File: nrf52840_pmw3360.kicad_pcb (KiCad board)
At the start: 2 copper layers, 18 x 33 mm, 3 parts, among them J1 PMW3360_Breakout, J2 Battery_JST-PH, U1 SuperMini_nRF52840

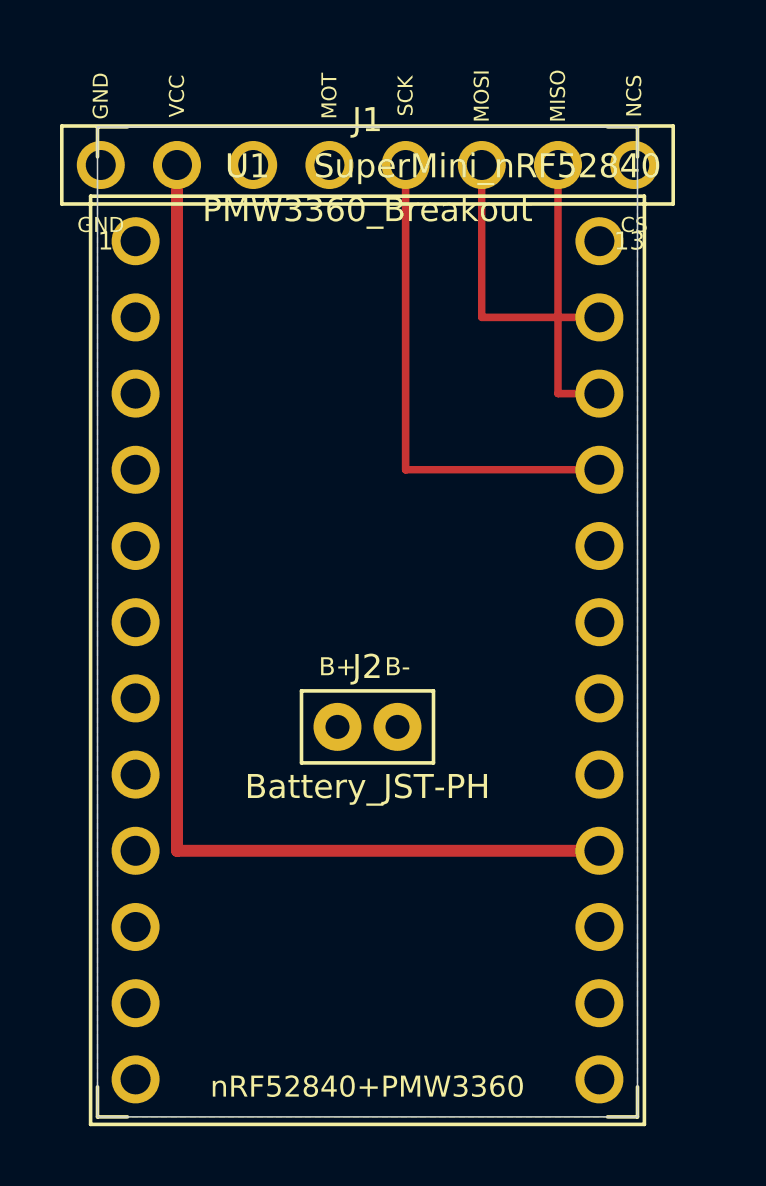
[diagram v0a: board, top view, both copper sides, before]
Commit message: feat: NCS・MOTION・BATIN未配線ネットをPCBに配線
- NCS: J1[8]→B.Cu右端→底辺→U1Lpin12 (周回ルート)
- MOTION: J1[4]→B.Cu縦→U1Lpin11 (L字ルート)
- BATIN: J2[1]→F.Cu縦→U1Rpin24 (L字ルート)
- J2バッテリーコネクタ: 左中央(x=4.5, y=16.5mm)に配置
- 全ネット配線完了: MOSI/MISO/SCK/VCC/BATIN(F.Cu) + NCS/MOTION(B.Cu)

Co-Authored-By: Claude Sonnet 4.6 <noreply@anthropic.com>
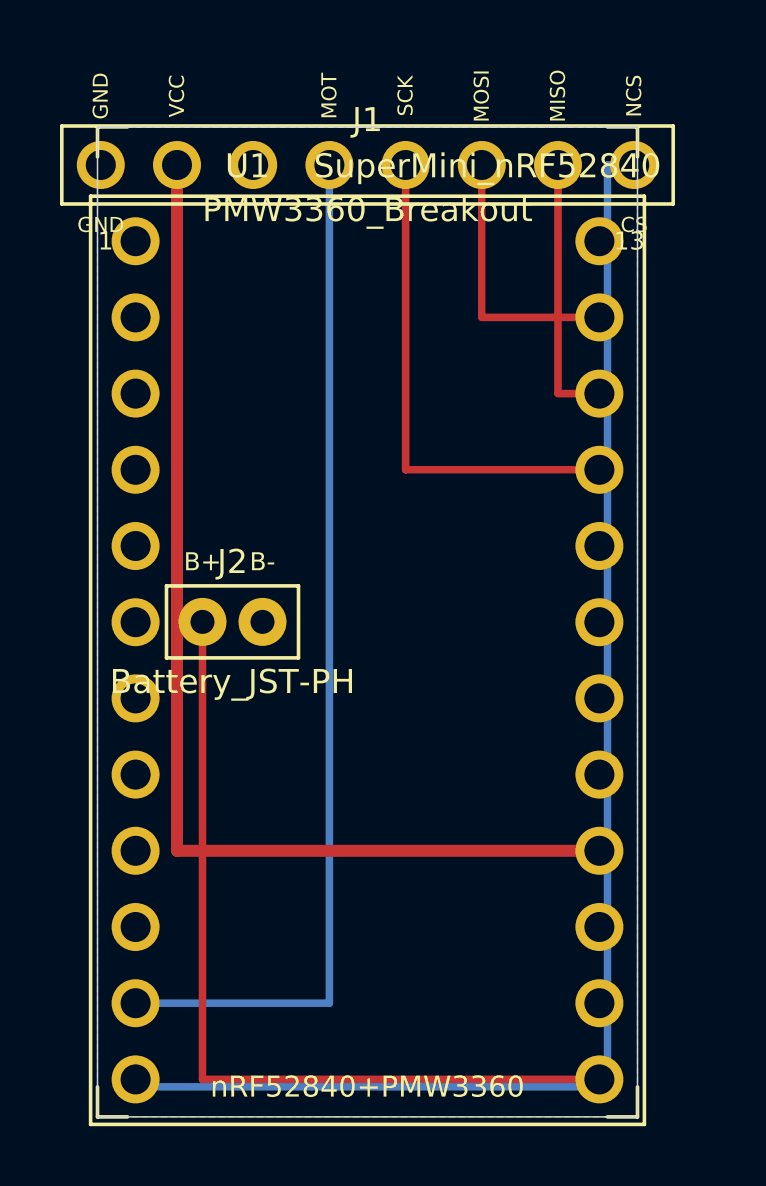
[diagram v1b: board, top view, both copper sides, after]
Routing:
- net NCS: track 0.00 -> 47.6 mm
- net MOTION: track 0.00 -> 34.4 mm
- net BATIN: track 0.00 -> 28.5 mm
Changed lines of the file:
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@@
 )
 (footprint "Connector_JST_PH_2pin" (layer "F.Cu") (at 0 0)
-  (fp_text reference "J2" (at 9.0000 18.0000) (layer "F.SilkS")
+  (fp_text reference "J2" (at 4.5000 14.5000) (layer "F.SilkS")
     (effects (font (size 0.8 0.8) (thickness 0.15))))
-  (fp_text value "Battery_JST-PH" (at 9.0000 22.0000) (layer "F.SilkS")
+  (fp_text value "Battery_JST-PH" (at 4.5000 18.5000) (layer "F.SilkS")
     (effects (font (size 0.8 0.8) (thickness 0.15))))
-    (pad "1" thru_hole oval (at 8.0000 20.0000) (size 1.6000 1.6000) (drill 0.8000) (layers "*.Cu" "*.Mask") (net 8 "BATIN"))
-    (pad "2" thru_hole circle (at 10.0000 20.0000) (size 1.6000 1.6000) (drill 0.8000) (layers "*.Cu" "*.Mask") (net 1 "GND"))
-  (fp_line (start 6.5500 18.5500) (end 11.4500 18.5500) (stroke (width 0.0500) (type default)) (layer "F.CrtYd"))
-  (fp_line (start 11.4500 18.5500) (end 11.4500 21.4500) (stroke (width 0.0500) (type default)) (layer "F.CrtYd"))
-  (fp_line (start 11.4500 21.4500) (end 6.5500 21.4500) (stroke (width 0.0500) (type default)) (layer "F.CrtYd"))
-  (fp_line (start 6.5500 21.4500) (end 6.5500 18.5500) (stroke (width 0.0500) (type default)) (layer "F.CrtYd"))
-  (fp_line (start 6.8000 18.8000) (end 11.2000 18.8000) (stroke (width 0.1200) (type default)) (layer "F.SilkS"))
-  (fp_line (start 11.2000 18.8000) (end 11.2000 21.2000) (stroke (width 0.1200) (type default)) (layer "F.SilkS"))
-  (fp_line (start 11.2000 21.2000) (end 6.8000 21.2000) (stroke (width 0.1200) (type default)) (layer "F.SilkS"))
-  (fp_line (start 6.8000 21.2000) (end 6.8000 18.8000) (stroke (width 0.1200) (type default)) (layer "F.SilkS"))
-  (fp_text user "B+" (at 8.0000 18.0000) (layer "F.SilkS")
+    (pad "1" thru_hole oval (at 3.5000 16.5000) (size 1.6000 1.6000) (drill 0.8000) (layers "*.Cu" "*.Mask") (net 8 "BATIN"))
+    (pad "2" thru_hole circle (at 5.5000 16.5000) (size 1.6000 1.6000) (drill 0.8000) (layers "*.Cu" "*.Mask") (net 1 "GND"))
+  (fp_line (start 2.0500 15.0500) (end 6.9500 15.0500) (stroke (width 0.0500) (type default)) (layer "F.CrtYd"))
+  (fp_line (start 6.9500 15.0500) (end 6.9500 17.9500) (stroke (width 0.0500) (type default)) (layer "F.CrtYd"))
+  (fp_line (start 6.9500 17.9500) (end 2.0500 17.9500) (stroke (width 0.0500) (type default)) (layer "F.CrtYd"))
+  (fp_line (start 2.0500 17.9500) (end 2.0500 15.0500) (stroke (width 0.0500) (type default)) (layer "F.CrtYd"))
+  (fp_line (start 2.3000 15.3000) (end 6.7000 15.3000) (stroke (width 0.1200) (type default)) (layer "F.SilkS"))
+  (fp_line (start 6.7000 15.3000) (end 6.7000 17.7000) (stroke (width 0.1200) (type default)) (layer "F.SilkS"))
+  (fp_line (start 6.7000 17.7000) (end 2.3000 17.7000) (stroke (width 0.1200) (type default)) (layer "F.SilkS"))
+  (fp_line (start 2.3000 17.7000) (end 2.3000 15.3000) (stroke (width 0.1200) (type default)) (layer "F.SilkS"))
+  (fp_text user "B+" (at 3.5000 14.5000) (layer "F.SilkS")
     (effects (font (size 0.6 0.6) (thickness 0.15))))
-  (fp_text user "B-" (at 10.0000 18.0000) (layer "F.SilkS")
+  (fp_text user "B-" (at 5.5000 14.5000) (layer "F.SilkS")
     (effects (font (size 0.6 0.6) (thickness 0.15))))
 )
@@
 (segment (start 2.6500 1.2700) (end 2.6500 24.1300) (width 0.4000) (layer "F.Cu") (net 2))
 (segment (start 2.6500 24.1300) (end 16.7300 24.1300) (width 0.4000) (layer "F.Cu") (net 2))
+(segment (start 3.5000 16.5000) (end 3.5000 31.7500) (width 0.2500) (layer "F.Cu") (net 8))
+(segment (start 3.5000 31.7500) (end 16.7300 31.7500) (width 0.2500) (layer "F.Cu") (net 8))
+(segment (start 17.8900 1.2700) (end 17.0000 1.2700) (width 0.2500) (layer "B.Cu") (net 6))
+(segment (start 17.0000 1.2700) (end 17.0000 32.0000) (width 0.2500) (layer "B.Cu") (net 6))
+(segment (start 17.0000 32.0000) (end 1.2700 32.0000) (width 0.2500) (layer "B.Cu") (net 6))
+(segment (start 1.2700 32.0000) (end 1.2700 31.7500) (width 0.2500) (layer "B.Cu") (net 6))
+(segment (start 7.7300 1.2700) (end 7.7300 29.2100) (width 0.2500) (layer "B.Cu") (net 7))
+(segment (start 7.7300 29.2100) (end 1.2700 29.2100) (width 0.2500) (layer "B.Cu") (net 7))
 (zone (net 1) (net_name "GND") (layer "B.Cu")
   (hatch edge 0.508)

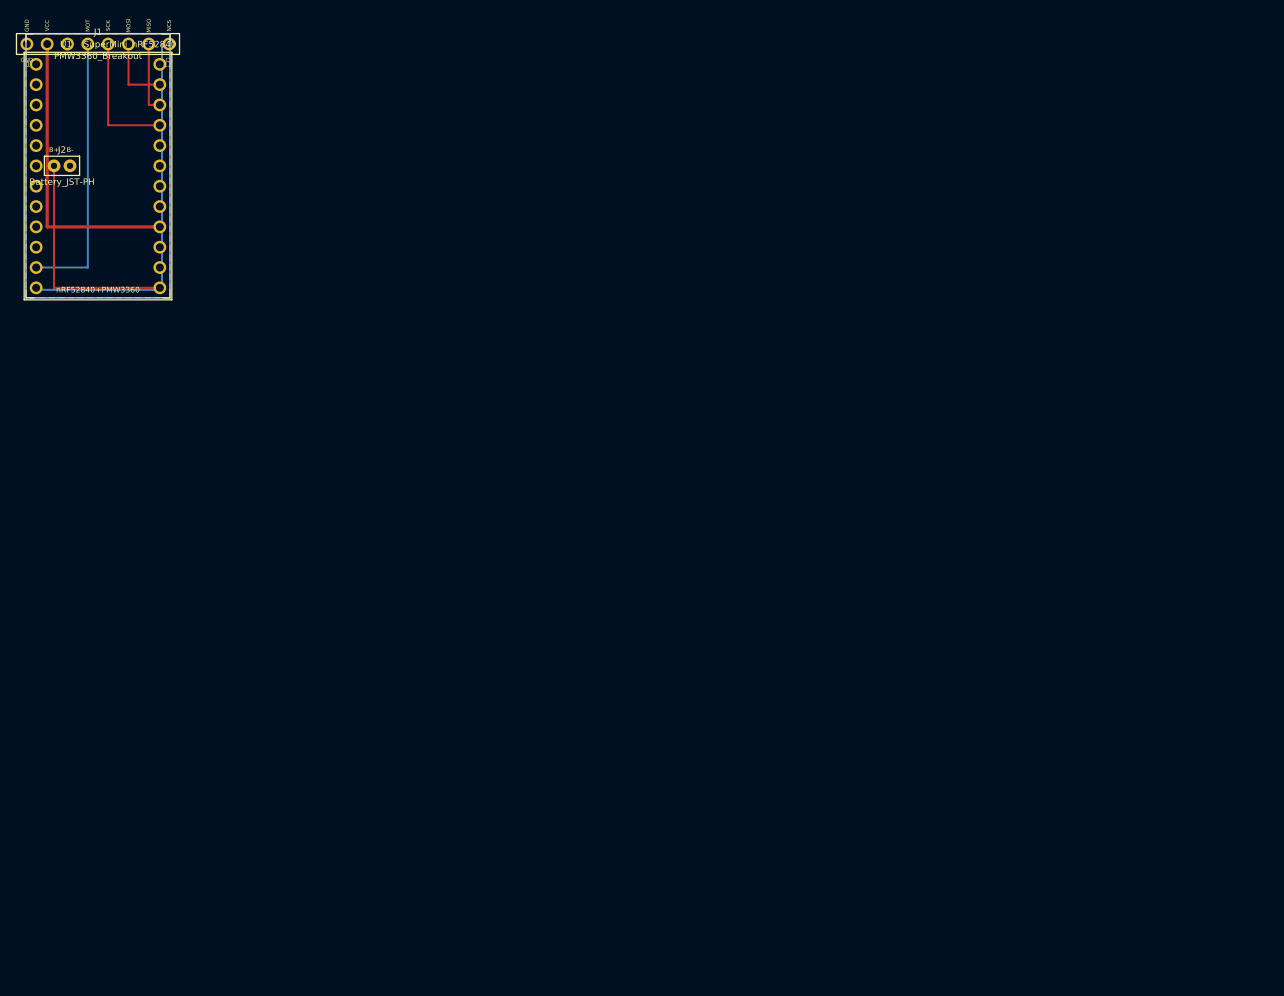
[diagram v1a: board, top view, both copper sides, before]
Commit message: fix: ボードをA4ページ中央(135,85mm)に配置、左上表示を修正
KiCadで開いたとき原点(0,0)＝左上隅に表示される問題を修正。
ORIGIN_X=135, ORIGIN_Y=85 のオフセットを全座標に適用。

Co-Authored-By: Claude Sonnet 4.6 <noreply@anthropic.com>
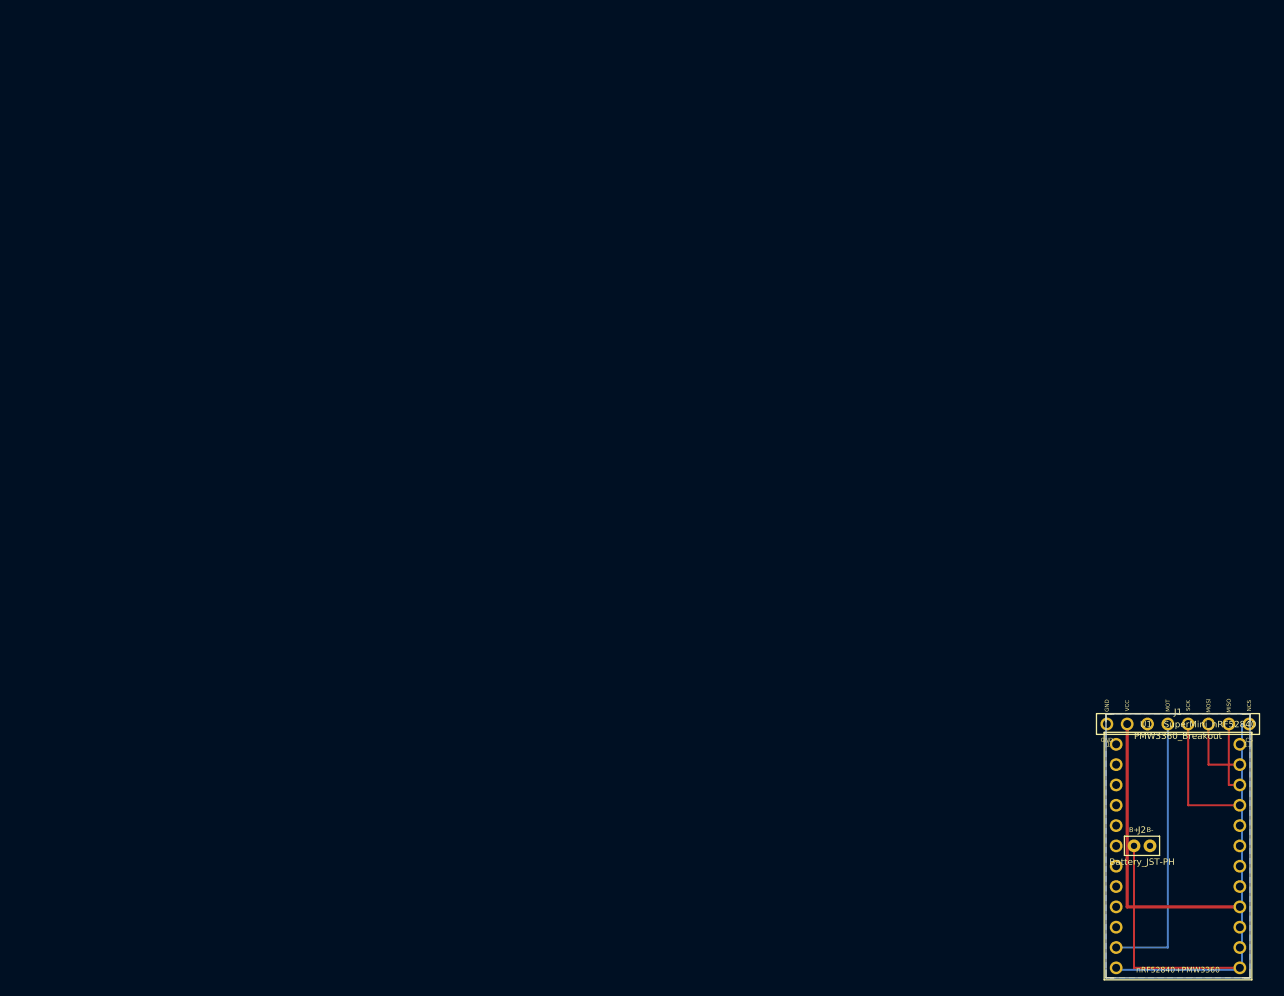
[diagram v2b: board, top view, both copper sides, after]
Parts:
- moved J1 159.5 mm to (135.0, 85.0)
- moved J2 159.5 mm to (135.0, 85.0)
- moved U1 159.5 mm to (135.0, 85.0)
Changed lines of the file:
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@@
   (net 7 "MOTION")
   (net 8 "BATIN")
-  (gr_rect (start 0 0) (end 18.0000 33.0000) (stroke (width 0.05) (type default)) (layer "Edge.Cuts"))
-  (gr_line (start 0.00 0.00) (end 1.00 0.00) (stroke (width 0.12) (type default)) (layer "F.SilkS"))
-  (gr_line (start 0.00 0.00) (end 0.00 1.00) (stroke (width 0.12) (type default)) (layer "F.SilkS"))
-  (gr_line (start 18.00 0.00) (end 17.00 0.00) (stroke (width 0.12) (type default)) (layer "F.SilkS"))
-  (gr_line (start 18.00 0.00) (end 18.00 1.00) (stroke (width 0.12) (type default)) (layer "F.SilkS"))
-  (gr_line (start 18.00 33.00) (end 17.00 33.00) (stroke (width 0.12) (type default)) (layer "F.SilkS"))
-  (gr_line (start 18.00 33.00) (end 18.00 32.00) (stroke (width 0.12) (type default)) (layer "F.SilkS"))
-  (gr_line (start 0.00 33.00) (end 1.00 33.00) (stroke (width 0.12) (type default)) (layer "F.SilkS"))
-  (gr_line (start 0.00 33.00) (end 0.00 32.00) (stroke (width 0.12) (type default)) (layer "F.SilkS"))
-(footprint "SuperMini_nRF52840_Socket" (layer "F.Cu") (at 0 0)
+  (gr_rect (start 135.0000 85.0000) (end 153.0000 118.0000) (stroke (width 0.05) (type default)) (layer "Edge.Cuts"))
+  (gr_line (start 135.00 85.00) (end 136.00 85.00) (stroke (width 0.12) (type default)) (layer "F.SilkS"))
+  (gr_line (start 135.00 85.00) (end 135.00 86.00) (stroke (width 0.12) (type default)) (layer "F.SilkS"))
+  (gr_line (start 153.00 85.00) (end 152.00 85.00) (stroke (width 0.12) (type default)) (layer "F.SilkS"))
+  (gr_line (start 153.00 85.00) (end 153.00 86.00) (stroke (width 0.12) (type default)) (layer "F.SilkS"))
+  (gr_line (start 153.00 118.00) (end 152.00 118.00) (stroke (width 0.12) (type default)) (layer "F.SilkS"))
+  (gr_line (start 153.00 118.00) (end 153.00 117.00) (stroke (width 0.12) (type default)) (layer "F.SilkS"))
+  (gr_line (start 135.00 118.00) (end 136.00 118.00) (stroke (width 0.12) (type default)) (layer "F.SilkS"))
+  (gr_line (start 135.00 118.00) (end 135.00 117.00) (stroke (width 0.12) (type default)) (layer "F.SilkS"))
+(footprint "SuperMini_nRF52840_Socket" (layer "F.Cu") (at 135.0000 85.0000)
   (fp_text reference "U1" (at 5.0000 1.3100) (layer "F.SilkS")
     (effects (font (size 0.8 0.8) (thickness 0.15))))
@@
     (effects (font (size 0.6 0.6) (thickness 0.15))))
 )
-(footprint "Connector_PinHeader_2.54mm_1x08" (layer "F.Cu") (at 0 0)
+(footprint "Connector_PinHeader_2.54mm_1x08" (layer "F.Cu") (at 135.0000 85.0000)
   (fp_text reference "J1" (at 9.0000 -0.2300) (layer "F.SilkS")
     (effects (font (size 0.8 0.8) (thickness 0.15))))
@@
     (effects (font (size 0.5 0.5) (thickness 0.15))))
 )
-(footprint "Connector_JST_PH_2pin" (layer "F.Cu") (at 0 0)
+(footprint "Connector_JST_PH_2pin" (layer "F.Cu") (at 135.0000 85.0000)
   (fp_text reference "J2" (at 4.5000 14.5000) (layer "F.SilkS")
     (effects (font (size 0.8 0.8) (thickness 0.15))))
@@
     (effects (font (size 0.6 0.6) (thickness 0.15))))
 )
-(segment (start 12.8100 1.2700) (end 12.8100 6.3500) (width 0.2500) (layer "F.Cu") (net 3))
-(segment (start 12.8100 6.3500) (end 16.7300 6.3500) (width 0.2500) (layer "F.Cu") (net 3))
-(segment (start 15.3500 1.2700) (end 15.3500 8.8900) (width 0.2500) (layer "F.Cu") (net 4))
-(segment (start 15.3500 8.8900) (end 16.7300 8.8900) (width 0.2500) (layer "F.Cu") (net 4))
-(segment (start 10.2700 1.2700) (end 10.2700 11.4300) (width 0.2500) (layer "F.Cu") (net 5))
-(segment (start 10.2700 11.4300) (end 16.7300 11.4300) (width 0.2500) (layer "F.Cu") (net 5))
-(segment (start 2.6500 1.2700) (end 2.6500 24.1300) (width 0.4000) (layer "F.Cu") (net 2))
-(segment (start 2.6500 24.1300) (end 16.7300 24.1300) (width 0.4000) (layer "F.Cu") (net 2))
-(segment (start 3.5000 16.5000) (end 3.5000 31.7500) (width 0.2500) (layer "F.Cu") (net 8))
-(segment (start 3.5000 31.7500) (end 16.7300 31.7500) (width 0.2500) (layer "F.Cu") (net 8))
-(segment (start 17.8900 1.2700) (end 17.0000 1.2700) (width 0.2500) (layer "B.Cu") (net 6))
-(segment (start 17.0000 1.2700) (end 17.0000 32.0000) (width 0.2500) (layer "B.Cu") (net 6))
-(segment (start 17.0000 32.0000) (end 1.2700 32.0000) (width 0.2500) (layer "B.Cu") (net 6))
-(segment (start 1.2700 32.0000) (end 1.2700 31.7500) (width 0.2500) (layer "B.Cu") (net 6))
-(segment (start 7.7300 1.2700) (end 7.7300 29.2100) (width 0.2500) (layer "B.Cu") (net 7))
-(segment (start 7.7300 29.2100) (end 1.2700 29.2100) (width 0.2500) (layer "B.Cu") (net 7))
+(segment (start 147.8100 86.2700) (end 147.8100 91.3500) (width 0.2500) (layer "F.Cu") (net 3))
+(segment (start 147.8100 91.3500) (end 151.7300 91.3500) (width 0.2500) (layer "F.Cu") (net 3))
+(segment (start 150.3500 86.2700) (end 150.3500 93.8900) (width 0.2500) (layer "F.Cu") (net 4))
+(segment (start 150.3500 93.8900) (end 151.7300 93.8900) (width 0.2500) (layer "F.Cu") (net 4))
+(segment (start 145.2700 86.2700) (end 145.2700 96.4300) (width 0.2500) (layer "F.Cu") (net 5))
+(segment (start 145.2700 96.4300) (end 151.7300 96.4300) (width 0.2500) (layer "F.Cu") (net 5))
+(segment (start 137.6500 86.2700) (end 137.6500 109.1300) (width 0.4000) (layer "F.Cu") (net 2))
+(segment (start 137.6500 109.1300) (end 151.7300 109.1300) (width 0.4000) (layer "F.Cu") (net 2))
+(segment (start 138.5000 101.5000) (end 138.5000 116.7500) (width 0.2500) (layer "F.Cu") (net 8))
+(segment (start 138.5000 116.7500) (end 151.7300 116.7500) (width 0.2500) (layer "F.Cu") (net 8))
+(segment (start 152.8900 86.2700) (end 152.0000 86.2700) (width 0.2500) (layer "B.Cu") (net 6))
+(segment (start 152.0000 86.2700) (end 152.0000 117.0000) (width 0.2500) (layer "B.Cu") (net 6))
+(segment (start 152.0000 117.0000) (end 136.2700 117.0000) (width 0.2500) (layer "B.Cu") (net 6))
+(segment (start 136.2700 117.0000) (end 136.2700 116.7500) (width 0.2500) (layer "B.Cu") (net 6))
+(segment (start 142.7300 86.2700) (end 142.7300 114.2100) (width 0.2500) (layer "B.Cu") (net 7))
+(segment (start 142.7300 114.2100) (end 136.2700 114.2100) (width 0.2500) (layer "B.Cu") (net 7))
 (zone (net 1) (net_name "GND") (layer "B.Cu")
   (hatch edge 0.508)
@@
   (fill yes (thermal_gap 0.5) (thermal_bridge_width 0.5))
   (polygon (pts
-    (xy 0.0 0.0) (xy 18.0000 0.0)
-    (xy 18.0000 33.0000) (xy 0.0 33.0000)))
+    (xy 135.0000 85.0000) (xy 153.0000 85.0000)
+    (xy 153.0000 118.0000) (xy 135.0000 118.0000)))
 )
-(gr_text "nRF52840+PMW3360" (at 9.0000 32.0000 0) (layer "F.SilkS")
+(gr_text "nRF52840+PMW3360" (at 144.0000 117.0000 0) (layer "F.SilkS")
   (effects (font (size 0.7 0.7) (thickness 0.15))))
-(gr_text "GND" (at 0.1100 -1.0300 90) (layer "F.SilkS")
+(gr_text "GND" (at 135.1100 83.9700 90) (layer "F.SilkS")
   (effects (font (size 0.5 0.5) (thickness 0.15))))
-(gr_text "VCC" (at 2.6500 -1.0300 90) (layer "F.SilkS")
+(gr_text "VCC" (at 137.6500 83.9700 90) (layer "F.SilkS")
   (effects (font (size 0.5 0.5) (thickness 0.15))))
-(gr_text "MOT" (at 7.7300 -1.0300 90) (layer "F.SilkS")
+(gr_text "MOT" (at 142.7300 83.9700 90) (layer "F.SilkS")
   (effects (font (size 0.5 0.5) (thickness 0.15))))
-(gr_text "SCK" (at 10.2700 -1.0300 90) (layer "F.SilkS")
+(gr_text "SCK" (at 145.2700 83.9700 90) (layer "F.SilkS")
   (effects (font (size 0.5 0.5) (thickness 0.15))))
-(gr_text "MOSI" (at 12.8100 -1.0300 90) (layer "F.SilkS")
+(gr_text "MOSI" (at 147.8100 83.9700 90) (layer "F.SilkS")
   (effects (font (size 0.5 0.5) (thickness 0.15))))
-(gr_text "MISO" (at 15.3500 -1.0300 90) (layer "F.SilkS")
+(gr_text "MISO" (at 150.3500 83.9700 90) (layer "F.SilkS")
   (effects (font (size 0.5 0.5) (thickness 0.15))))
-(gr_text "NCS" (at 17.8900 -1.0300 90) (layer "F.SilkS")
+(gr_text "NCS" (at 152.8900 83.9700 90) (layer "F.SilkS")
   (effects (font (size 0.5 0.5) (thickness 0.15))))
 )
